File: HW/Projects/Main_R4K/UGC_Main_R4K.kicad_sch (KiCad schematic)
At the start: 167 parts, among them J1 SM02B-SURS-TF_LF__SN_, J10 SM02B-SURS-TF_LF__SN_, J13 503480-0640, J2 503480-0640, J4 Conn_01x06_Pin, J5 UJ31-CH-G1-SMT-TR, J6 Trigger, J7 Trigger, J8 Conn_01x02, J9 Conn_01x02, Q1 MMBT3904, Q2 MMBT3904, Q3 BSS138DW, Q4 BSS138DW, Q5 MMBT2222A, Q6 MMBT2222A, SW1 1TS026A-1000-0550, SW1 SW_Push, SW10 SW_Push, SW11 SW_Push, SW12 SW_Push, SW13 SW_Push, SW14 TS-1187A-C-A-B, SW17 TS-1187A-C-A-B, SW18 TS-1187A-C-A-B, SW19 TS-1187A-C-A-B, SW2 SW_Push, SW3 SW_Push, SW4 SW_Push, SW5 TS-1187A-C-A-B, SW6 GL18_SW, SW7 SW_Push, SW8 SW_Push, SW9 TS-1187A-C-A-B, U1 ESP32-PICO-MINI-02, U10 ST_LSM6, U11 BQ25180, U12 CH340K, U13 PI3USB4000A, U2 GD25Q80EEIGR, U4 TPS630001RCR, U5 ST_LSM6, U6 MCP3002, U7 MCP3002, U8 RP2040, X1 ModConnect, X2 ModConnect, X3 ModConnect, X4 ModConnect, X5 ModConnect, X6 ModConnect, Y1 ABM8-272-T3

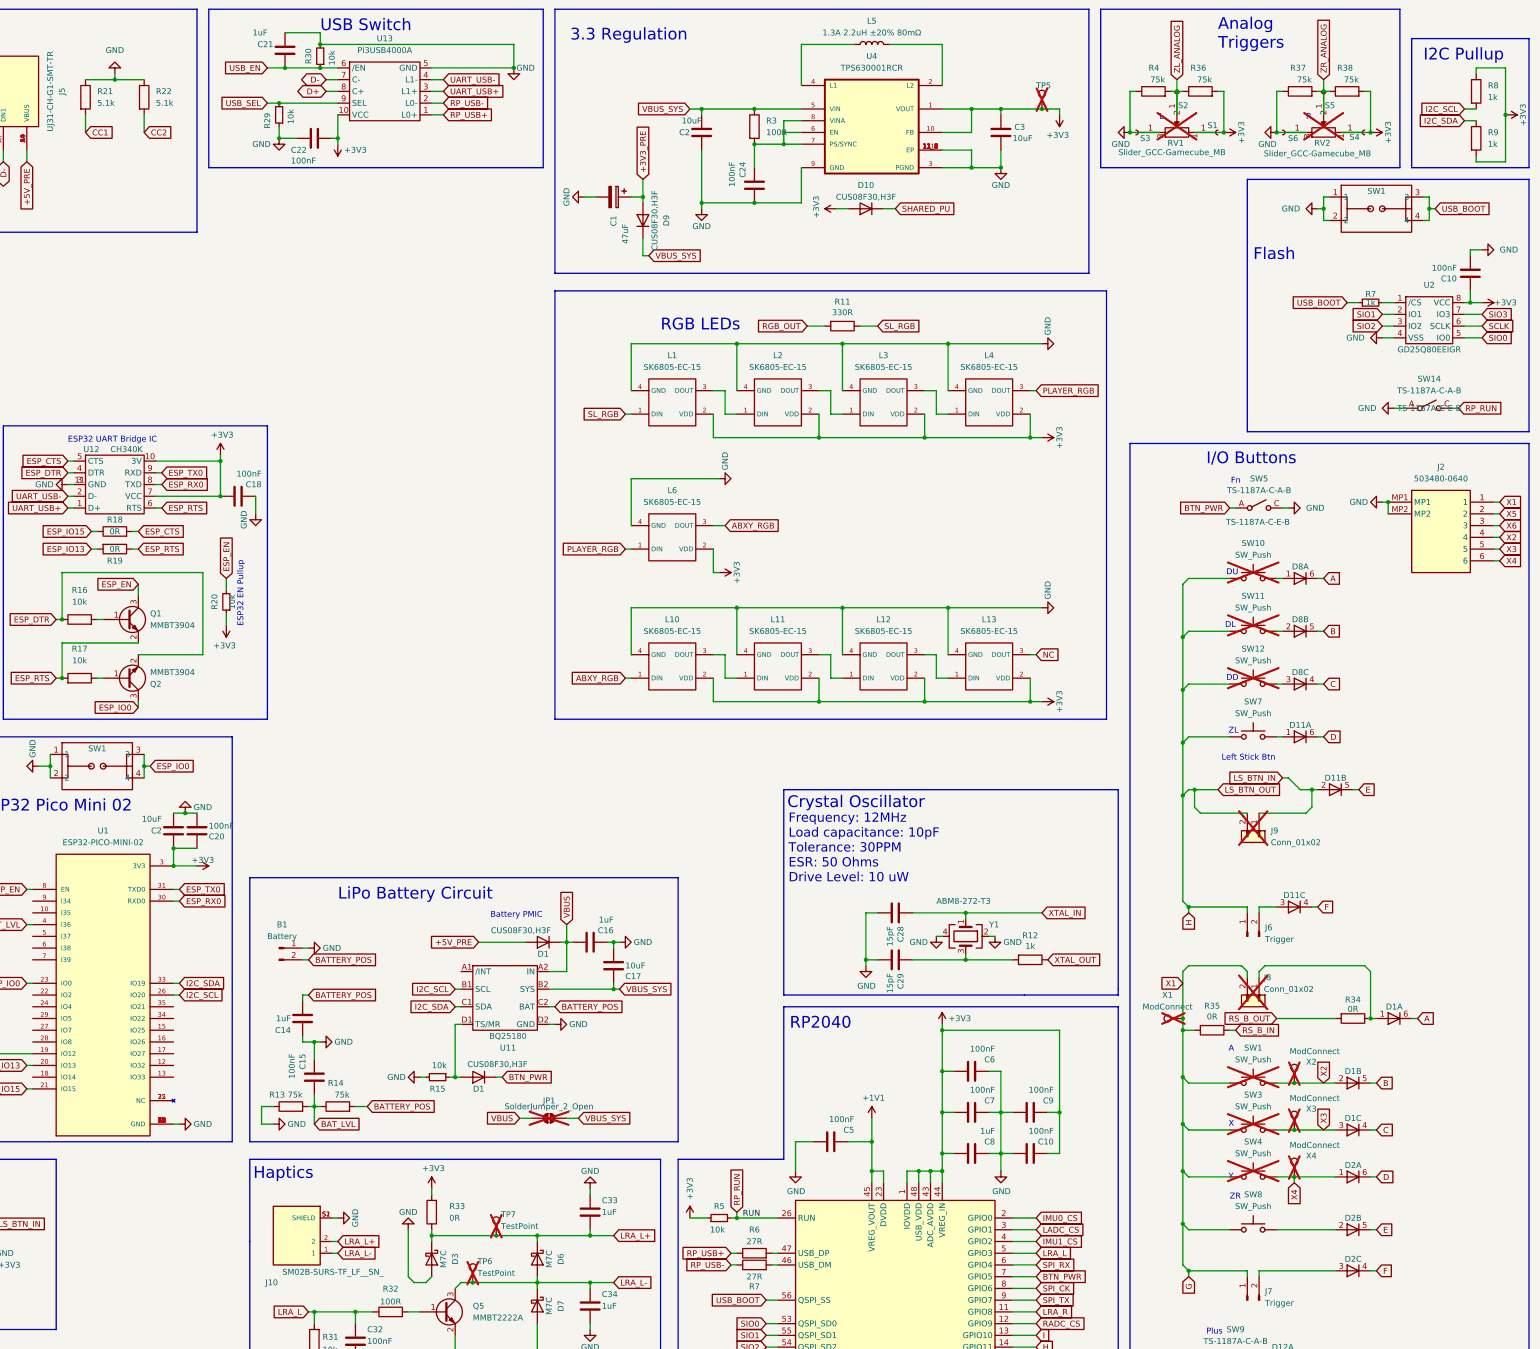
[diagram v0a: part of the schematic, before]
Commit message: GCU R5 Update
- Add fuel gauge IC
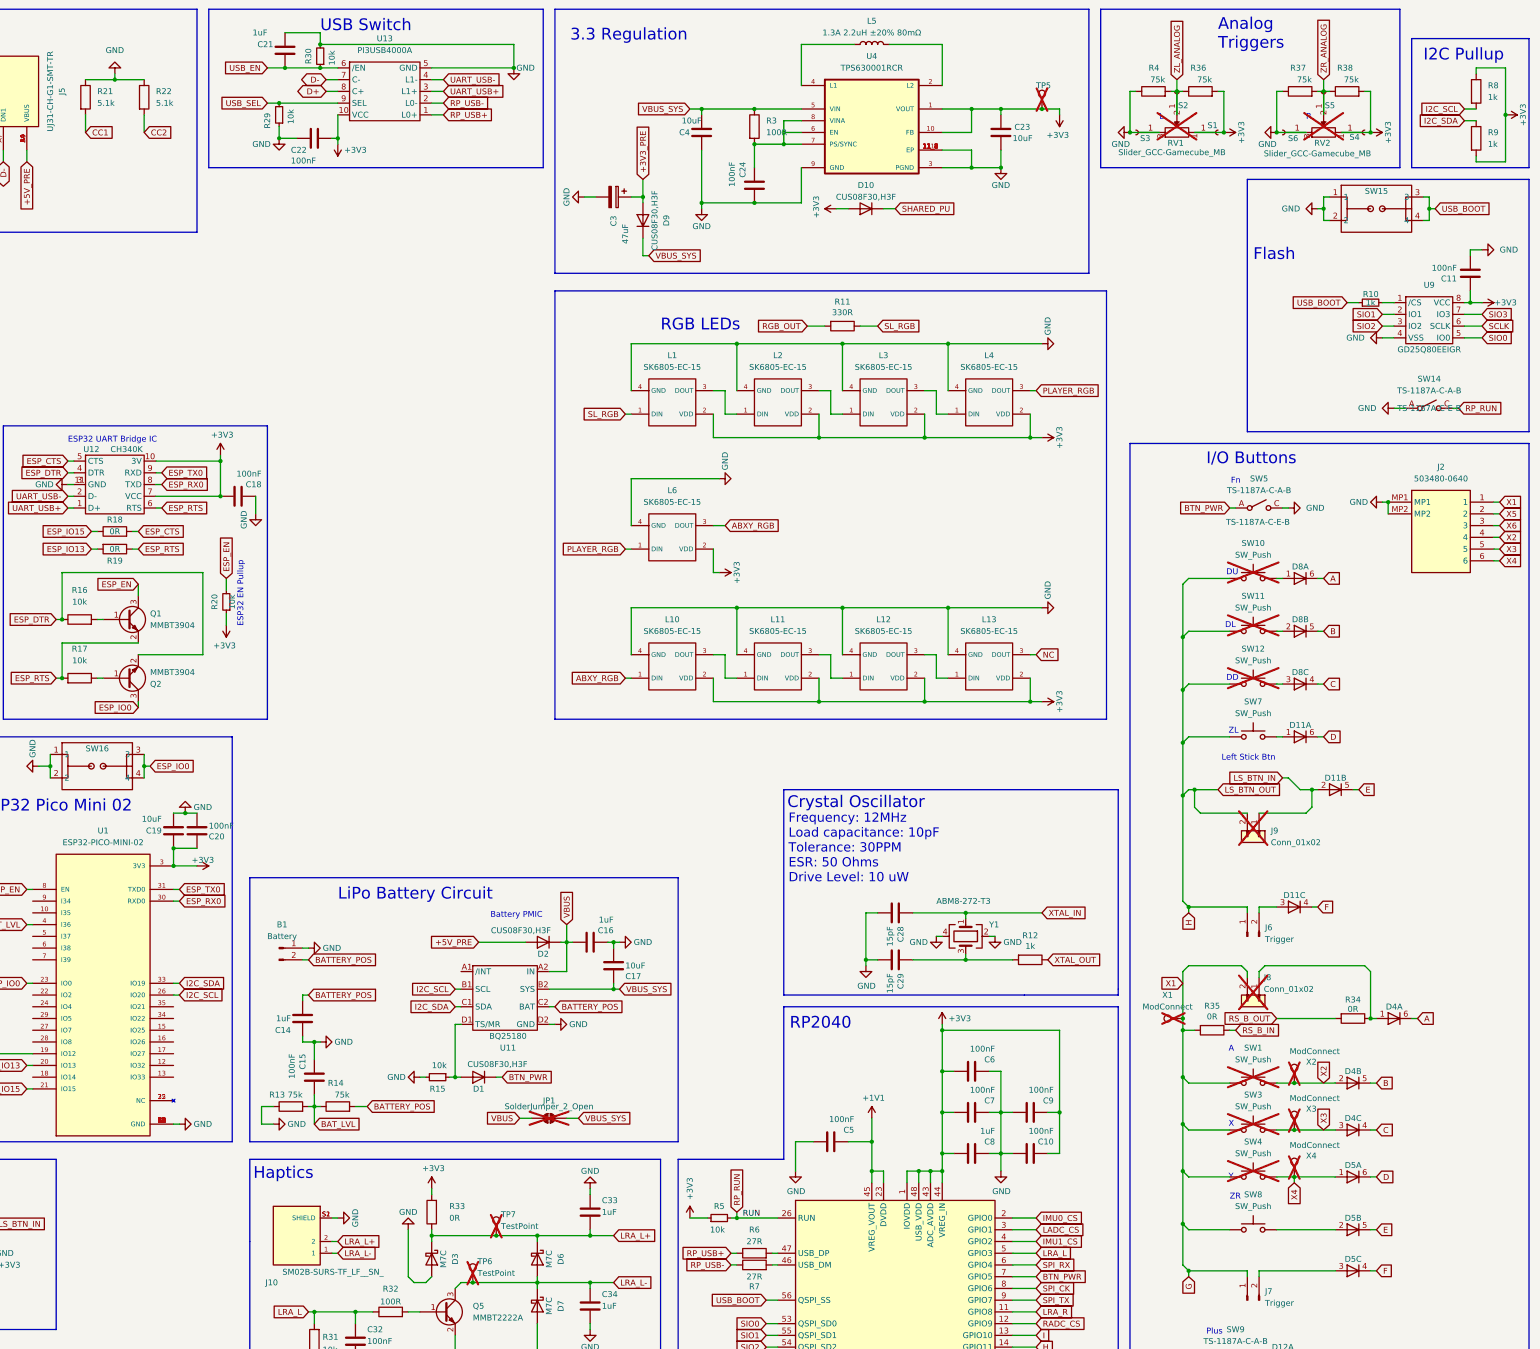
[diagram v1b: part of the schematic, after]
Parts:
- SW14, SW17, SW18, SW19, SW5, SW9: value TS-1187A-C-A-B -> TS-1187A-C-A-B
- renumbered C10 to C11, C2 to C19, C3 to C23, C1 to C3, C2 to C4, D1 to D2, D1 to D4, D2 to D5, R7 to R10, SW1 to SW15, SW1 to SW16, U2 to U9
